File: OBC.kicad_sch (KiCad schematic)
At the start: 27 parts, among them J1 SQT-110-01-L-D, J2 54-00175, U1 OEM719

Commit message: Continue PCB layout
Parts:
- removed AE1: Antenna, Connector_Coaxial:SMA_Amphenol_901-144_Vertical, symbol Device:Antenna
- removed J2: 54-00175, 54_00175-audio-jack:TENSILITY_54-00175, symbol 54-00175-audio-jack:54-00175
- added J2: 81_MMBX-S50-0-18, symbol Connector:Conn_Coaxial_Small
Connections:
- net UART_F_RX is gone; now on net GNSS_RXD1: H1OBC1.44
- net UART_F_TX is gone; now on net GNSS_TXD1: H1OBC1.42
- net GND: now also U1.22 (GND), U1.23 (GND), U1.24 (GND), U1.25 (GND), J2.2 (Ext)
- net at U1.21 (ANT): now also J2.1 (In)
- no-connect marks 212 -> 208
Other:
- note added: "CM4 UART4"
- note added: "CM4 UART5"
- note added: "OEM719B UART1 (CONFIG)"
- note added: "SPACECRAFT BUS CONNECTIONS"
- note removed: "GNSS CONFIG"
- note removed: "SPACECRAFT BUS MAPPINGS"
- note removed: "UART4"
- note removed: "UART5"
- moved on the sheet: J1, JP1, JP2, R7, R8

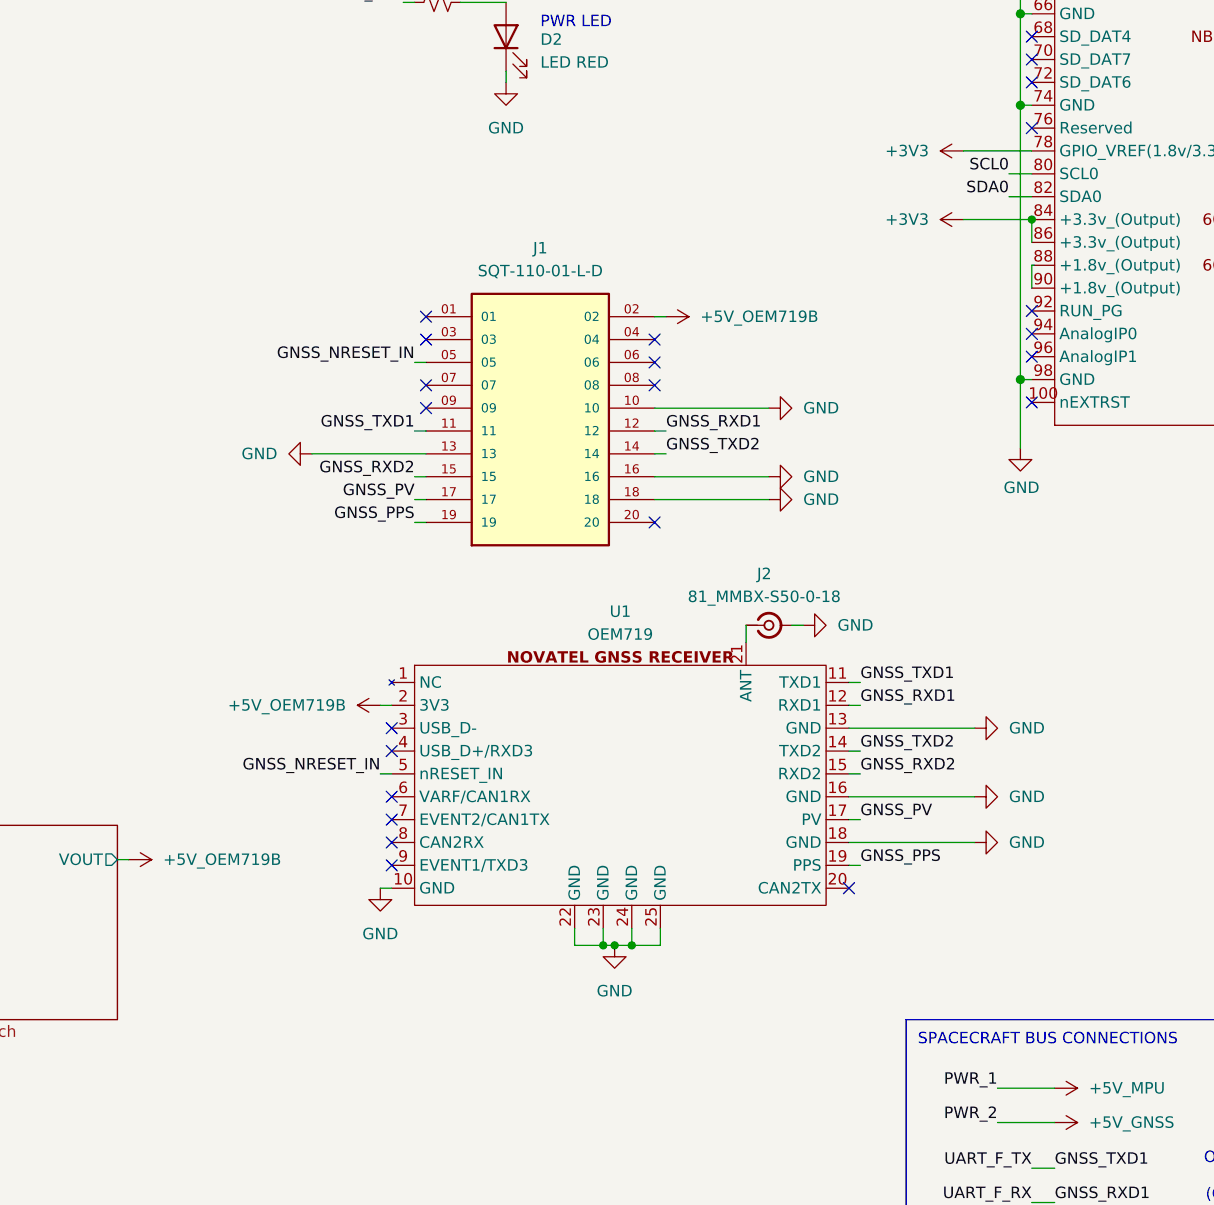
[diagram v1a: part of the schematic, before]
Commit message: OBC: complete layout first pass
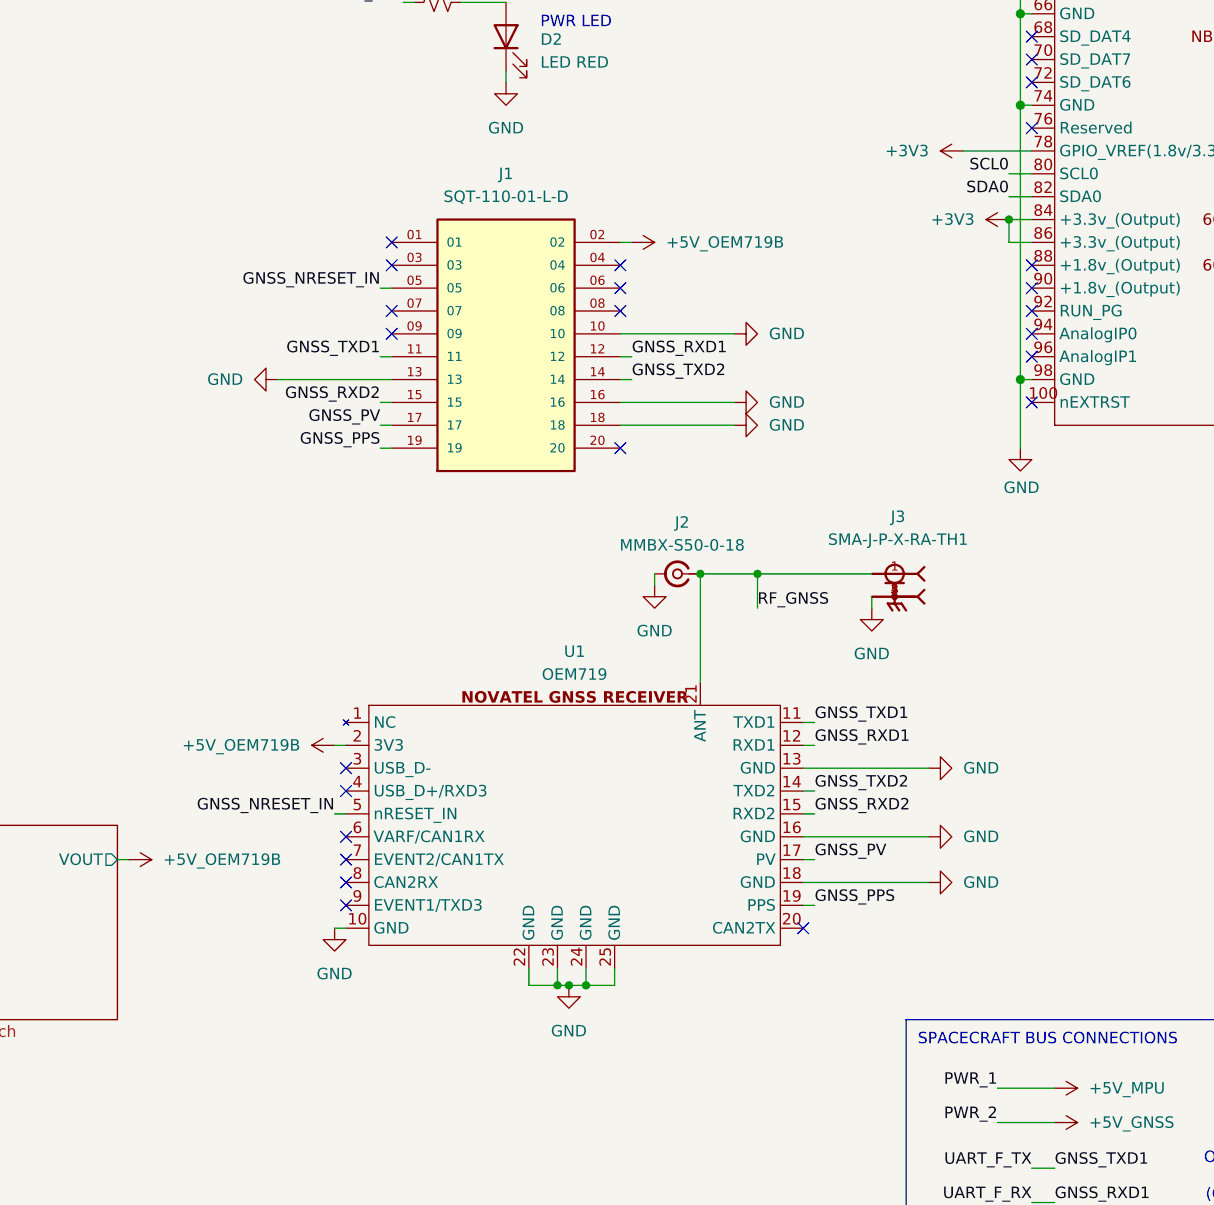
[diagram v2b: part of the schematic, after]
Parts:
- removed J2: 81_MMBX-S50-0-18, symbol Connector:Conn_Coaxial_Small
- added J2: MMBX-S50-0-18, Novatel:MMBX-S50-0-18, symbol Novatel:MMBX-S50-0-18
- added J3: SMA-J-P-X-RA-TH1, SMA_J_P_H_RA_TH1:SAMTEC_SMA-J-P-X-RA-TH1, symbol SMA-J-P-X-RA-TH1:SMA-J-P-X-RA-TH1
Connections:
- net GND: now also J2.2 (Ext), J3.2, J3.3, J3.4, J3.5
- net RF_GNSS: now reaches U1.21 (ANT)
- net RF_GNSS: now also J2.1 (In), J3.1
- net at Module1.88 (+1.8v_(Output)): no longer Module1.90 (+1.8v_(Output))
- no-connect marks 208 -> 210
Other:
- moved on the sheet: J1, U1

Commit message: Layout confirmed, PCBs ordered
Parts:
- C1, C2: DigiKey Part Number (none) -> 720-GA0805Y104JXABT31GCT-ND
- D1: DigiKey Part Number (none) -> 160-1179-1-ND
- D2: DigiKey Part Number (none) -> 160-1427-1-ND
- J1: DigiKey Part Number (none) -> SAM1245-10-ND
- J2: DigiKey Part Number (none) -> 3628-82_MMBX-S50-0-1/111_NMCT-ND
- Module1: DigiKey Part Number (none) -> H11615CT-ND
- R1, R2, R3, R4: DigiKey Part Number (none) -> RMCF0805FT60R4CT-ND
- R10, R9: DigiKey Part Number P4.70KHCT-ND -> RMCF0805JT47K0CT-ND
- R5: DigiKey Part Number (none) -> P39ACT-ND
- R6: DigiKey Part Number (none) -> 311-45.3CRCT-ND
- R7, R8: DigiKey Part Number (none) -> 541-2.10KCCT-ND
- U1: now not fitted
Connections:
- net CHARGE: now also H1OBC1.31, H1OBC1.32; no longer H2OBC1.43, H2OBC1.44
- net DS_A: now also H2OBC1.51; no longer H2OBC1.48
- net DS_B: now also H2OBC1.52; no longer H2OBC1.50
- net DS_C: now also H2OBC1.48; no longer H2OBC1.52
- net GND: now also H1OBC1.33, H1OBC1.34; no longer H1OBC1.29, H1OBC1.30, H1OBC1.31, H1OBC1.32
- net RBF_A: now also H2OBC1.49; no longer H2OBC1.47
- net RBF_B: now also H2OBC1.50; no longer H2OBC1.49
- net RBF_C: now also H2OBC1.47; no longer H2OBC1.51
- no-connect marks 210 -> 214
